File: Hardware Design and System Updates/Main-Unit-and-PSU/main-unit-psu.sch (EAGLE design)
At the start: 28 parts, among them U1 BA033CC0FP-E2TO252-3_ROM, U2 BA033CC0FP-E2TO252-3_ROM, U3 MSP430FR2110IPW16, U4 TLR342F-GE2SOP8_ROM, U5 TMP36GT9ZT_3_ADI

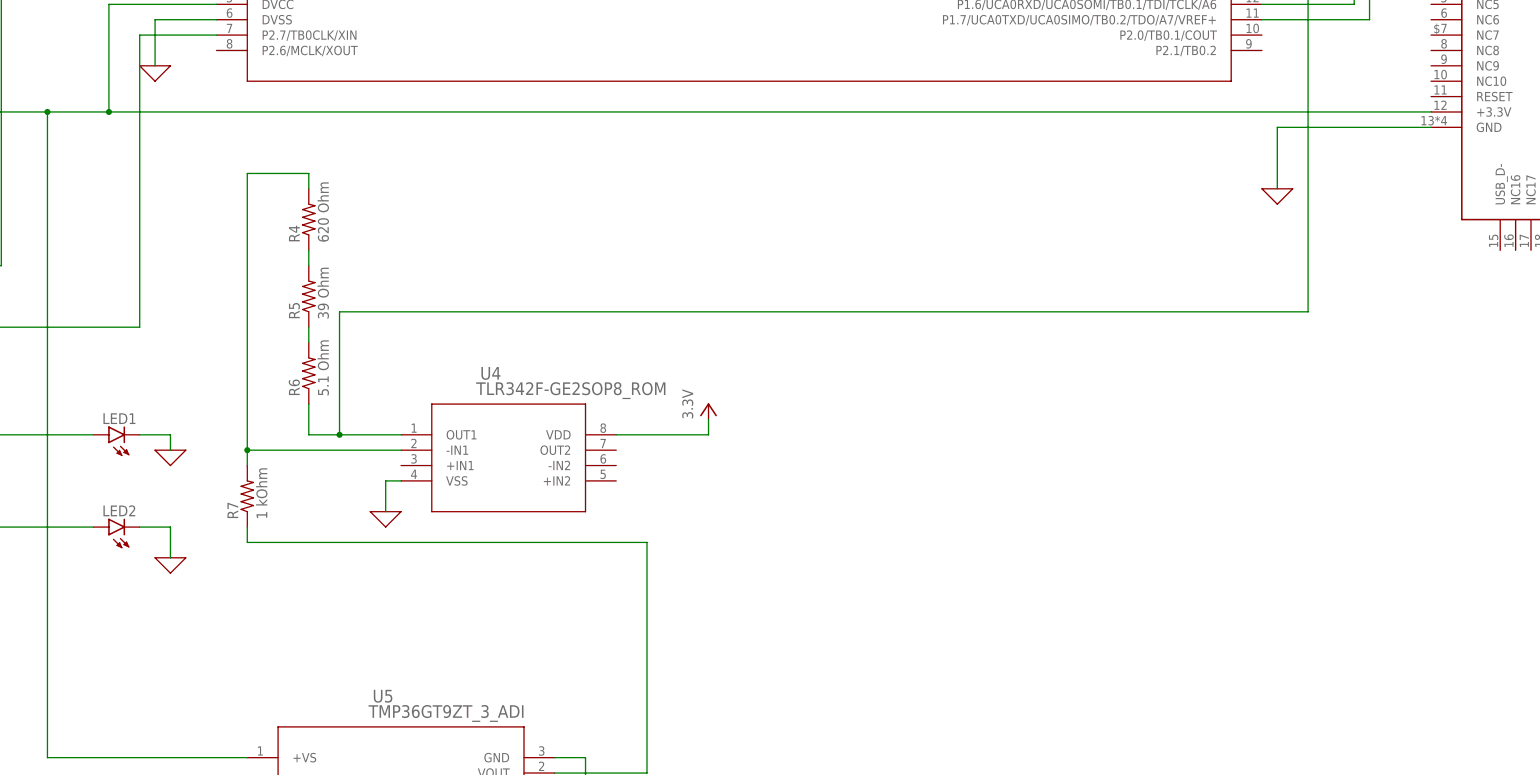
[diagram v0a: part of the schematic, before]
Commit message: Added 5v regulator to schematics
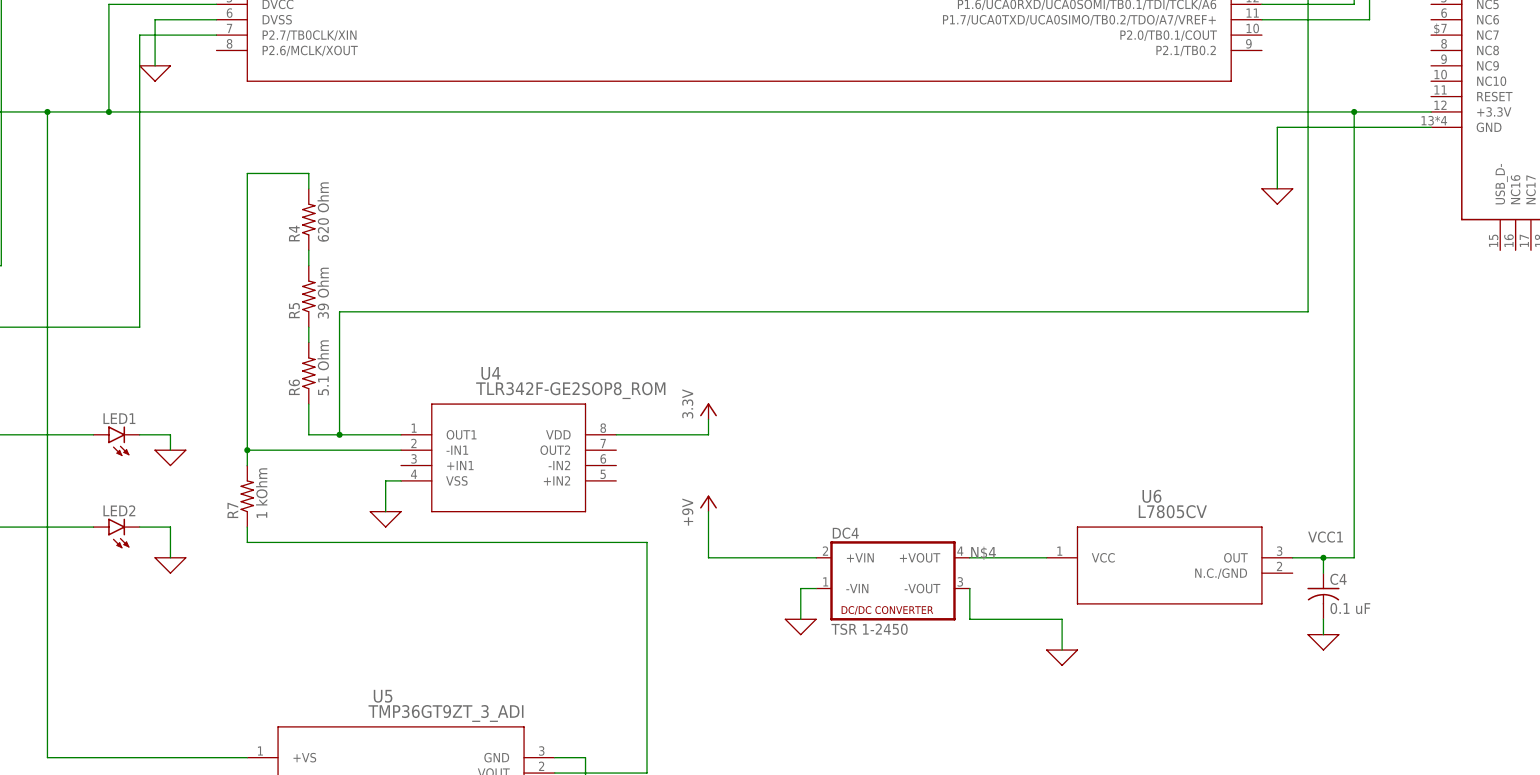
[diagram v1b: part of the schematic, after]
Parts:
- added C4: 0.1 uF, rcl:C-US050-024X044
- added DC4: TSR 1-2450, dc-dc-converter:NME
- added U6: L7805CV, 2023-03-08_12-17-23_Library:BA033CC0FP-E2TO252-3_ROM
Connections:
- new net +5V: DC4.+VIN
- net 0: now also C4.2, DC4.-VIN, DC4.-VOUT
- net N$4: now also DC4.+VOUT, U6.VCC
- net VCC1: now also C4.1, U6.OUT
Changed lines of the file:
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@@
 <part name="U5" library="2023-03-28_14-12-25_Library" deviceset="TMP36GT9Z" device="T_3_ADI"/>
 <part name="X_18" library="ngspice-simulation" library_urn="urn:adsk.eagle:library:527439" deviceset="GND" device=""/>
+<part name="DC4" library="dc-dc-converter" library_urn="urn:adsk.eagle:library:208" deviceset="NME" device="" package3d_urn="urn:adsk.eagle:package:12313/1" value="TSR 1-2450"/>
+<part name="X_17" library="ngspice-simulation" library_urn="urn:adsk.eagle:library:527439" deviceset="GND" device=""/>
+<part name="U6" library="2023-03-08_12-17-23_Library" deviceset="BA033CC0FP-E2" device="TO252-3_ROM" value="L7805CV"/>
+<part name="X_19" library="ngspice-simulation" library_urn="urn:adsk.eagle:library:527439" deviceset="GND" device=""/>
+<part name="C4" library="rcl" library_urn="urn:adsk.eagle:library:334" deviceset="C-US" device="050-024X044" package3d_urn="urn:adsk.eagle:package:23643/1" value="0.1 uF"/>
+<part name="X_20" library="ngspice-simulation" library_urn="urn:adsk.eagle:library:527439" deviceset="GND" device=""/>
+<part name="P+3" library="supply1" library_urn="urn:adsk.eagle:library:371" deviceset="+5V" device="" value="+9V"/>
 </parts>
 <sheets>
@@
 </instance>
 <instance part="X_18" gate="G$1" x="309.88" y="-60.96" smashed="yes"/>
+<instance part="DC4" gate="G$1" x="360.68" y="-20.32" smashed="yes">
+<attribute name="NAME" x="350.52" y="-14.605" size="1.778" layer="95"/>
+<attribute name="VALUE" x="350.52" y="-30.48" size="1.778" layer="96"/>
+</instance>
+<instance part="X_17" gate="G$1" x="345.44" y="-27.94" smashed="yes"/>
+<instance part="U6" gate="A" x="383.54" y="-17.78" smashed="yes">
+<attribute name="NAME" x="401.6746" y="-8.6614" size="2.083" layer="95" ratio="6"/>
+<attribute name="VALUE" x="401.0352" y="-11.2014" size="2.083" layer="96" ratio="6"/>
+</instance>
+<instance part="X_19" gate="G$1" x="388.62" y="-33.02" smashed="yes"/>
+<instance part="C4" gate="G$1" x="431.8" y="-22.86" smashed="yes">
+<attribute name="NAME" x="432.816" y="-22.225" size="1.778" layer="95"/>
+<attribute name="VALUE" x="432.816" y="-27.051" size="1.778" layer="96"/>
+</instance>
+<instance part="X_20" gate="G$1" x="431.8" y="-30.48" smashed="yes"/>
+<instance part="P+3" gate="1" x="330.2" y="-7.62" smashed="yes">
+<attribute name="VALUE" x="327.66" y="-12.7" size="1.778" layer="96" rot="R90"/>
+</instance>
 </instances>
 <busses>
@@
 <pinref part="X_18" gate="G$1" pin="0"/>
 </segment>
+<segment>
+<pinref part="X_17" gate="G$1" pin="0"/>
+<pinref part="DC4" gate="G$1" pin="-VIN"/>
+<wire x1="345.44" y1="-27.94" x2="345.44" y2="-22.86" width="0.1524" layer="91"/>
+<wire x1="345.44" y1="-22.86" x2="347.98" y2="-22.86" width="0.1524" layer="91"/>
+</segment>
+<segment>
+<pinref part="DC4" gate="G$1" pin="-VOUT"/>
+<wire x1="373.38" y1="-22.86" x2="373.38" y2="-27.94" width="0.1524" layer="91"/>
+<wire x1="373.38" y1="-27.94" x2="388.62" y2="-27.94" width="0.1524" layer="91"/>
+<pinref part="X_19" gate="G$1" pin="0"/>
+<wire x1="388.62" y1="-33.02" x2="388.62" y2="-27.94" width="0.1524" layer="91"/>
+</segment>
+<segment>
+<pinref part="X_20" gate="G$1" pin="0"/>
+<pinref part="C4" gate="G$1" pin="2"/>
+<wire x1="431.8" y1="-30.48" x2="431.8" y2="-27.94" width="0.1524" layer="91"/>
+</segment>
 </net>
 <net name="N$5" class="0">
@@
 <label x="137.16" y="55.88" size="1.778" layer="95"/>
 <pinref part="U1" gate="A" pin="VCC"/>
+</segment>
+<segment>
+<pinref part="DC4" gate="G$1" pin="+VOUT"/>
+<wire x1="373.38" y1="-17.78" x2="386.08" y2="-17.78" width="0.1524" layer="91"/>
+<label x="373.38" y="-17.78" size="1.778" layer="95"/>
+<pinref part="U6" gate="A" pin="VCC"/>
 </segment>
 </net>
@@
 <wire x1="231.14" y1="73.66" x2="231.14" y2="55.88" width="0.1524" layer="91"/>
 <pinref part="E1" gate="G$1" pin="+3.3V"/>
-<wire x1="231.14" y1="55.88" x2="449.58" y2="55.88" width="0.1524" layer="91"/>
+<wire x1="231.14" y1="55.88" x2="436.88" y2="55.88" width="0.1524" layer="91"/>
+<wire x1="436.88" y1="55.88" x2="449.58" y2="55.88" width="0.1524" layer="91"/>
 <wire x1="231.14" y1="55.88" x2="220.98" y2="55.88" width="0.1524" layer="91"/>
 <junction x="231.14" y="55.88"/>
@@
 <wire x1="220.98" y1="-50.8" x2="220.98" y2="55.88" width="0.1524" layer="91"/>
 <junction x="220.98" y="55.88"/>
+<wire x1="426.72" y1="-17.78" x2="431.8" y2="-17.78" width="0.1524" layer="91"/>
+<label x="429.26" y="-15.24" size="1.778" layer="95"/>
+<pinref part="U6" gate="A" pin="OUT"/>
+<pinref part="C4" gate="G$1" pin="1"/>
+<wire x1="431.8" y1="-20.32" x2="431.8" y2="-17.78" width="0.1524" layer="91"/>
+<junction x="431.8" y="-17.78"/>
+<wire x1="431.8" y1="-17.78" x2="436.88" y2="-17.78" width="0.1524" layer="91"/>
+<wire x1="436.88" y1="55.88" x2="436.88" y2="-17.78" width="0.1524" layer="91"/>
+<junction x="436.88" y="55.88"/>
 </segment>
 </net>
@@
 </segment>
 </net>
+<net name="+5V" class="0">
+<segment>
+<pinref part="DC4" gate="G$1" pin="+VIN"/>
+<wire x1="330.2" y1="-17.78" x2="347.98" y2="-17.78" width="0.1524" layer="91"/>
+<pinref part="P+3" gate="1" pin="+5V"/>
+<wire x1="330.2" y1="-17.78" x2="330.2" y2="-10.16" width="0.1524" layer="91"/>
+</segment>
+</net>

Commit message: Fixed system schematics
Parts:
- removed B1: KMB23S, rectifier:B-DIL
- removed C1: 470 uF, rcl:C-US050-024X044
- removed D2: NZX22C,133, diode:ZENER-DIODEDO41Z10
- removed DC3: R-78W9.0-0.5, dc-dc-converter:NME
- removed R2: 330 Ohm, rcl:R-US_0204/7
- removed TR1: TCT50-01E07AB, trafo:EE20-1
- added U7: RAC03-12SKRAC03-K_RCP, 2023-04-05_11-47-46_Library:RAC03-12SKRAC03-K_RCP
- R1: value 330 Ohm -> 65 Ohm
- U4: value TLR342F-GE2SOP8_ROM -> MCP6022-I/P; device 2023-03-28_11-48-47_Library:TLR342F-GE2SOP8_ROM -> MCP6022-I_P:MCP6022-I/P
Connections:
- removed net N$1: B1.AC1, TR1.S4
- removed net N$2: B1.AC2, TR1.S3
- removed net N$8: B1.+, C1.1, D2.C, DC3.+VIN
- net 0: now also U7.-VOUT; no longer B1.-, C1.2, D2.A, DC3.-VIN, DC3.-VOUT
- net N$11: now also U7.+VOUT; no longer DC3.+VOUT
- net N$16: no longer R2.2
- net N$20: now also U4.VOUTA; no longer U4.OUT1
- net N$21: now also U4.VINA+; no longer U4.-IN1
- net N$22: no longer R2.1
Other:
- moved on the sheet: R1, U4
